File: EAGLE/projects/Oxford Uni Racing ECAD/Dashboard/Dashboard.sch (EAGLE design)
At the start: 20 parts, among them J1 T821108A1S100CEU, J2 CAN_OUT, J3 PWR_CAN, J4 DISPL, J5 DISPL, K1 EC2-12NU, K2 EC2-12NU, X2 D-SUB9-H2M09ST

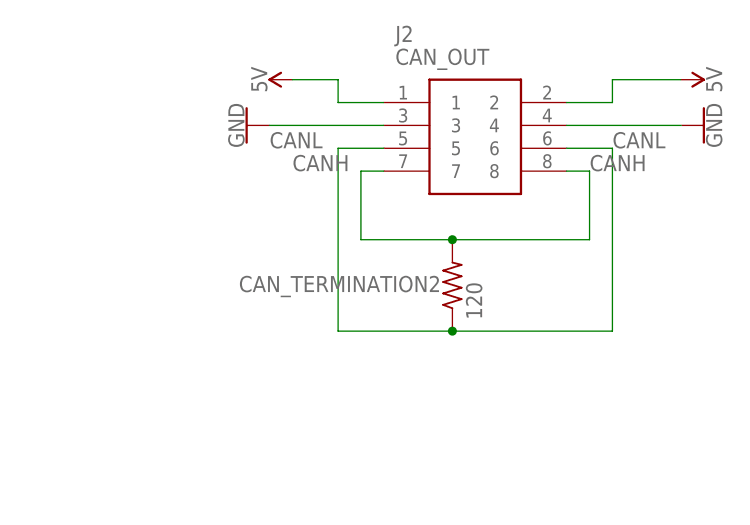
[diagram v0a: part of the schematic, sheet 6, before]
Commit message: removed redundant CAN termination resistor from dashboard
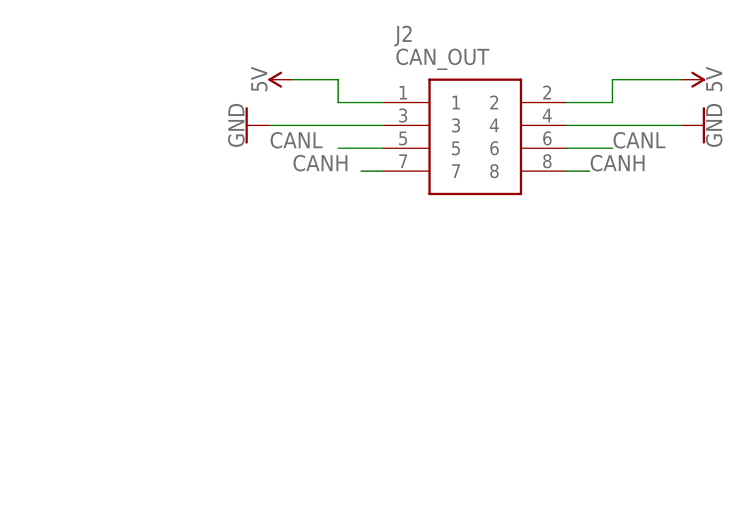
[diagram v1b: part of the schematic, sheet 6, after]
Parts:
- removed CAN_TERMINATION2: 120, adafruit:R-US_0204/7
- J5: value DISPL -> BUTTONS
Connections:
- net CANH: no longer CAN_TERMINATION2.2
- net CANL: no longer CAN_TERMINATION2.1
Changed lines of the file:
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@@
 <part name="GND15" library="SparkFun-PowerSymbols" library_urn="urn:adsk.eagle:library:530" deviceset="GND" device=""/>
 <part name="GND16" library="SparkFun-PowerSymbols" library_urn="urn:adsk.eagle:library:530" deviceset="GND" device=""/>
-<part name="CAN_TERMINATION2" library="adafruit" library_urn="urn:adsk.eagle:library:420" deviceset="R-US_" device="0204/7" package3d_urn="urn:adsk.eagle:package:6240596/1" value="120"/>
 <part name="J2" library="T821108A1S100CEU" deviceset="T821108A1S100CEU" device="" value="CAN_OUT"/>
 <part name="SUPPLY2" library="SparkFun-PowerSymbols" library_urn="urn:adsk.eagle:library:530" deviceset="5V" device=""/>
@@
 <part name="SUPPLY4" library="SparkFun-PowerSymbols" library_urn="urn:adsk.eagle:library:530" deviceset="5V" device=""/>
 <part name="GND17" library="SparkFun-PowerSymbols" library_urn="urn:adsk.eagle:library:530" deviceset="GND" device=""/>
-<part name="J5" library="T821108A1S100CEU" deviceset="T821108A1S100CEU" device="" value="DISPL"/>
+<part name="J5" library="T821108A1S100CEU" deviceset="T821108A1S100CEU" device="" value="BUTTONS"/>
 </parts>
 <sheets>
@@
 <attribute name="VALUE" x="86.106" y="73.66" size="1.778" layer="96" rot="R270" align="top-center"/>
 </instance>
-<instance part="CAN_TERMINATION2" gate="G$1" x="109.22" y="55.88" smashed="yes" rot="R90">
-<attribute name="NAME" x="107.95" y="56.9214" size="1.778" layer="95" rot="R180"/>
-<attribute name="VALUE" x="112.522" y="52.07" size="1.778" layer="96" rot="R90"/>
-</instance>
 <instance part="J2" gate="G$1" x="101.6" y="76.2" smashed="yes">
 <attribute name="NAME" x="102.87" y="83.82" size="1.778" layer="95" align="center-left"/>
@@
 <wire x1="121.92" y1="68.58" x2="124.46" y2="68.58" width="0.1524" layer="91"/>
 <label x="124.46" y="68.58" size="1.778" layer="95"/>
+<pinref part="J2" gate="G$1" pin="8"/>
+</segment>
+<segment>
+<pinref part="J2" gate="G$1" pin="7"/>
 <wire x1="101.6" y1="68.58" x2="99.06" y2="68.58" width="0.1524" layer="91"/>
 <label x="91.44" y="68.58" size="1.778" layer="95"/>
-<wire x1="99.06" y1="68.58" x2="99.06" y2="60.96" width="0.1524" layer="91"/>
-<pinref part="CAN_TERMINATION2" gate="G$1" pin="2"/>
-<wire x1="99.06" y1="60.96" x2="109.22" y2="60.96" width="0.1524" layer="91"/>
-<wire x1="124.46" y1="68.58" x2="124.46" y2="60.96" width="0.1524" layer="91"/>
-<wire x1="124.46" y1="60.96" x2="109.22" y2="60.96" width="0.1524" layer="91"/>
-<junction x="109.22" y="60.96"/>
-<pinref part="J2" gate="G$1" pin="7"/>
-<pinref part="J2" gate="G$1" pin="8"/>
 </segment>
 </net>
@@
 </segment>
 <segment>
-<label x="88.9" y="71.12" size="1.778" layer="95"/>
-<wire x1="101.6" y1="71.12" x2="96.52" y2="71.12" width="0.1524" layer="91"/>
-<wire x1="96.52" y1="71.12" x2="96.52" y2="50.8" width="0.1524" layer="91"/>
-<pinref part="CAN_TERMINATION2" gate="G$1" pin="1"/>
-<wire x1="96.52" y1="50.8" x2="109.22" y2="50.8" width="0.1524" layer="91"/>
-<wire x1="109.22" y1="50.8" x2="127" y2="50.8" width="0.1524" layer="91"/>
-<junction x="109.22" y="50.8"/>
-<wire x1="127" y1="50.8" x2="127" y2="71.12" width="0.1524" layer="91"/>
 <label x="127" y="71.12" size="1.778" layer="95"/>
 <wire x1="127" y1="71.12" x2="121.92" y2="71.12" width="0.1524" layer="91"/>
+<pinref part="J2" gate="G$1" pin="6"/>
+</segment>
+<segment>
 <pinref part="J2" gate="G$1" pin="5"/>
-<pinref part="J2" gate="G$1" pin="6"/>
-</segment>
-</net>
+<wire x1="101.6" y1="71.12" x2="96.52" y2="71.12" width="0.1524" layer="91"/>
+<label x="88.9" y="71.12" size="1.778" layer="95"/>
+</segment>
+</net>

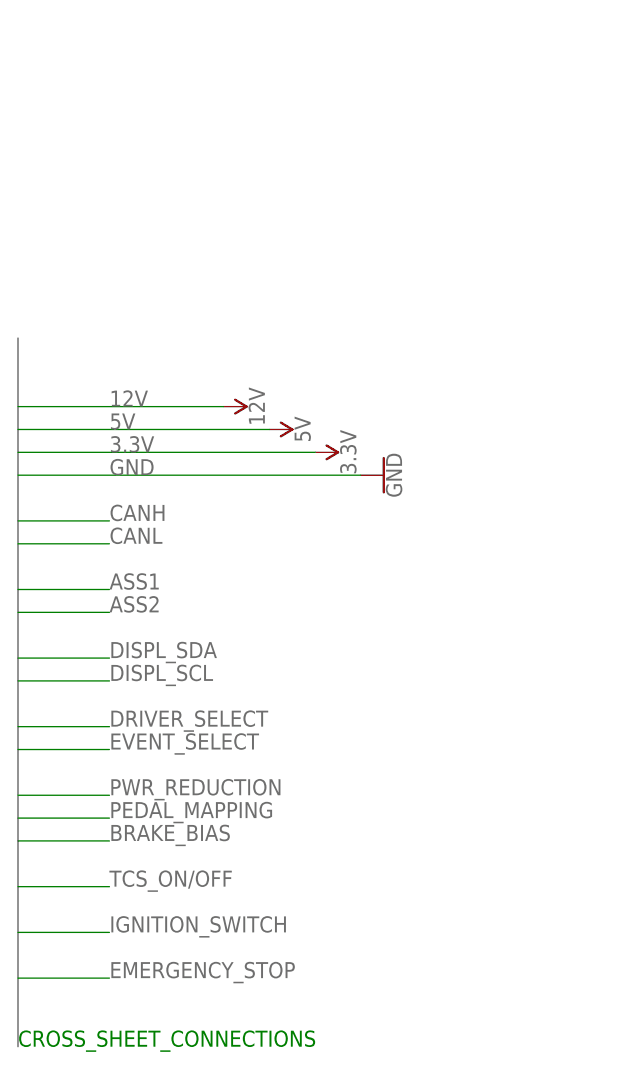
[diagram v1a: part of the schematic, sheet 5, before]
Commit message: updated buttons on all levels
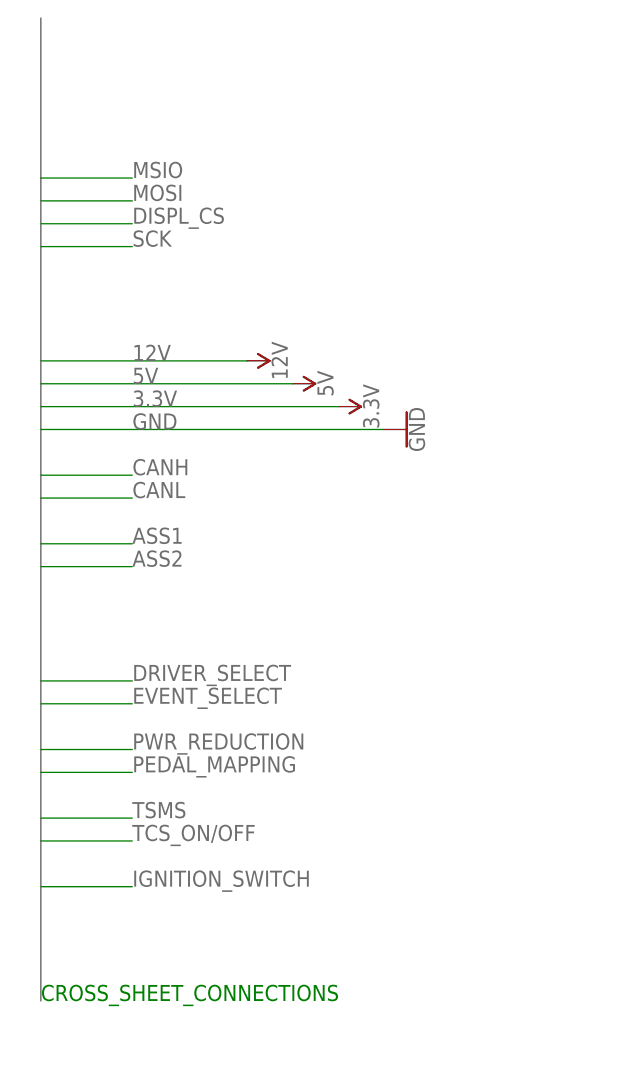
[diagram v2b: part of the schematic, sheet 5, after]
